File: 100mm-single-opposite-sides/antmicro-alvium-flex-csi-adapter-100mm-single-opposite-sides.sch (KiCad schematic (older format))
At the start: 3 parts, among them J1 WE_687622100002_FLEX, J2 WE_687650100002_FLEX

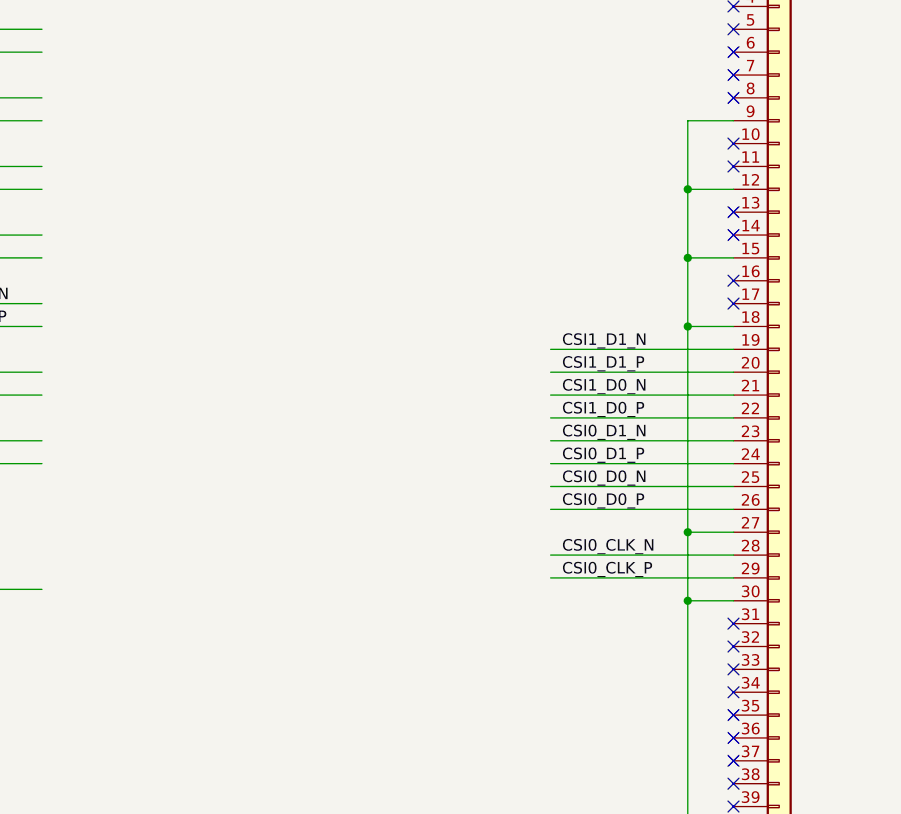
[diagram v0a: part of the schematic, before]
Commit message: 100mm-single-same: add NMOS transistor for camera triggering
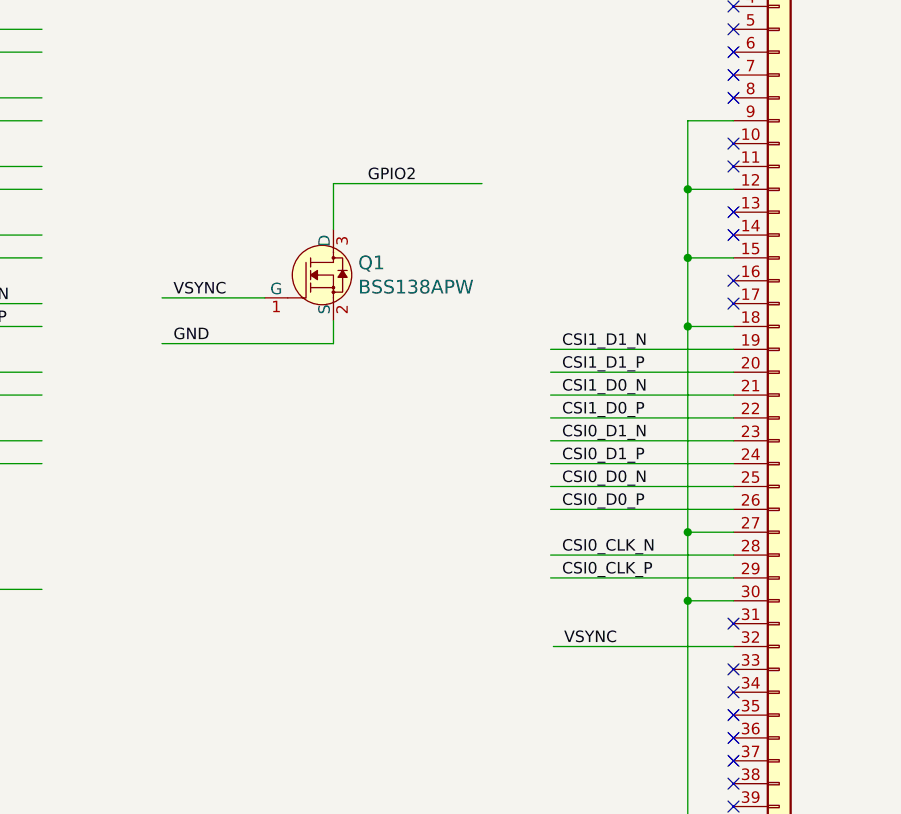
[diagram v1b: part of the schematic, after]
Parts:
- added Q1: BSS138APW, antmicro-alvium-flex-csi-adapter-footprints:SC70-3, symbol antmicro-alvium-flex-csi-adapter:BSS138APW
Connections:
- net labels added: VSYNC
- wire segments 61 -> 67
- no-connect marks 30 -> 29
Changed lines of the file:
@@
 Text Notes 925  1525 0    59   ~ 0
 Flexible PCB for connecting\nAllied Vision embedded vision cameras\nto Antmicro's hardware platforms using MIPI CSI-2 interface.
-NoConn ~ 9450 6575
 $Bitmap
 Pos 3100 10700
@@
 	1    0    0    -1
 $EndComp
+$Comp
+L antmicro-alvium-flex-csi-adapter:BSS138APW Q1
+U 1 1 5F8882DA
+P 7700 4950
+F 0 "Q1" H 7808 5003 60  0000 L CNN
+F 1 "BSS138APW" H 7808 4897 60  0000 L CNN
+F 2 "antmicro-alvium-flex-csi-adapter-footprints:SC70-3" H 7900 5150 60  0001 L CNN
+F 3 "" H 7900 5250 60  0001 L CNN
+F 4 "BSS138PW" H 7900 5450 60  0001 L CNN "MPN"
+F 5 "ON Semiconductor" H 7900 6050 60  0001 L CNN "Manufacturer"
+	1    7700 4950
+	1    0    0    -1
+$EndComp
+Wire Wire Line
+	7700 5150 7700 5250
+Wire Wire Line
+	7700 5250 6950 5250
+Wire Wire Line
+	7400 5050 6950 5050
+Wire Wire Line
+	7700 4750 7700 4550
+Wire Wire Line
+	7700 4550 8350 4550
+Text Label 7000 5250 0    50   ~ 0
+GND
+Text Label 7850 4550 0    50   ~ 0
+GPIO2
+Wire Wire Line
+	9450 6575 8662 6575
+Text Label 8709 6575 0    50   ~ 0
+VSYNC
+Text Label 7000 5050 0    50   ~ 0
+VSYNC
 $EndSCHEMATC
